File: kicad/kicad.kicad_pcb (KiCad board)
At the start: 2 copper layers, 50.8 x 25.4 mm, 13 parts, among them J1 USB_A_MALE, U1 MCP1702, U2 MCP6021

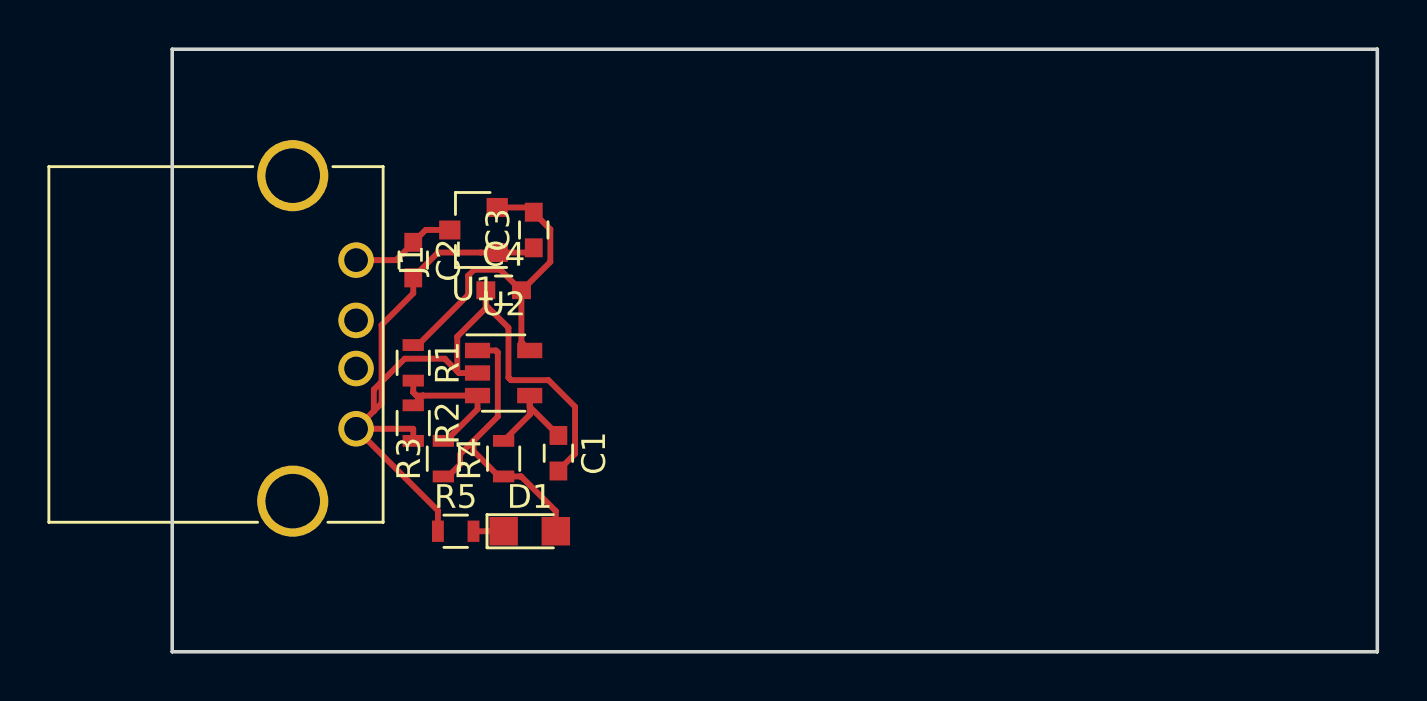
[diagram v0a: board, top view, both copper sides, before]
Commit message: Added fill of ground plane on front
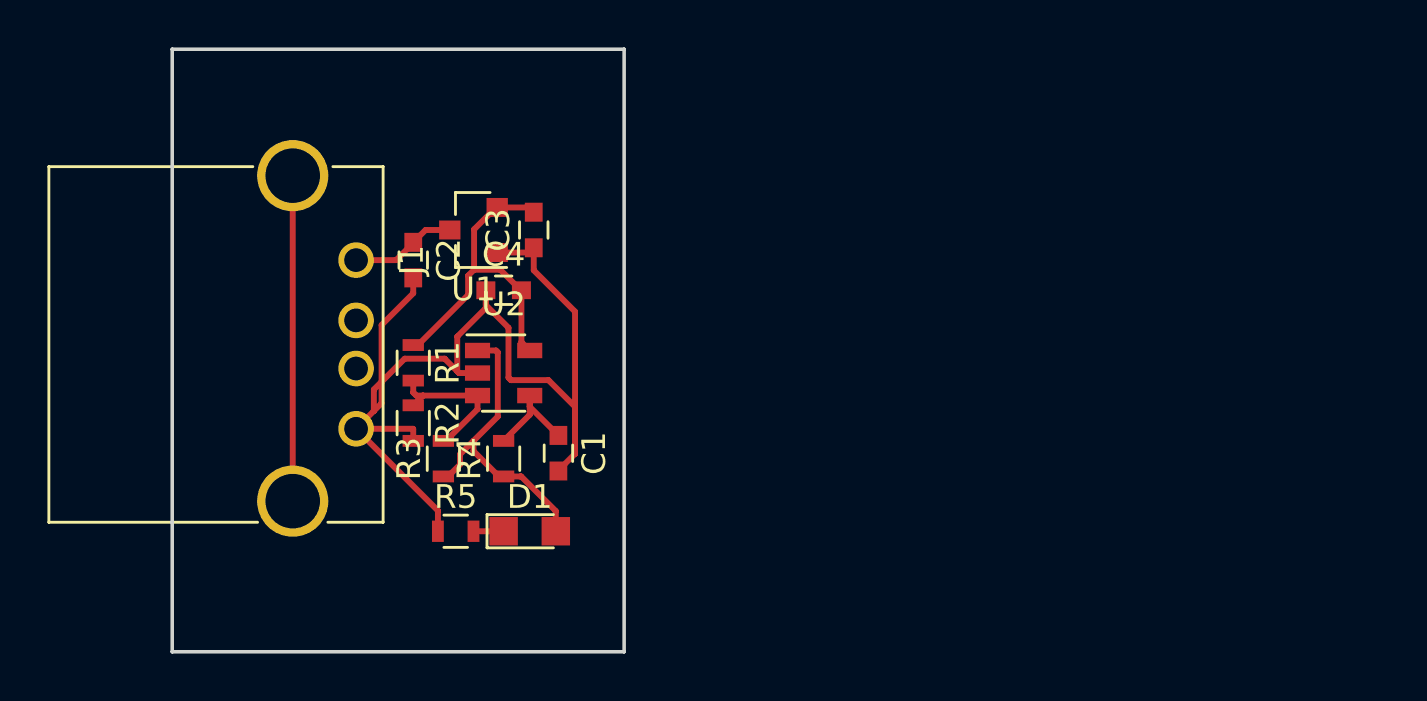
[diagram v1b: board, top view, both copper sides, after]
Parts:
- C2: value 1 uf -> 10 uf
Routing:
- net Net-(J1-Pad5): track 0.00 -> 13.7 mm
- net GND: track 42.1 -> 47.6 mm
- net +3V3: track 15.1 -> 14.1 mm
- added copper zone on F.Cu, net GND
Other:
- board size 50.8 x 25.4 mm -> 19.1 x 25.4 mm
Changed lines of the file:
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@@
   (general
     (links 24)
-    (no_connects 1)
-    (area 138.43 74.93 190.5 101.6)
+    (no_connects 0)
+    (area 139.624999 76.124999 190.575001 101.675001)
     (thickness 1.6)
     (drawings 4)
-    (tracks 83)
+    (tracks 84)
     (zones 0)
     (modules 13)
@@
     (47 F.CrtYd user)
     (48 B.Fab user)
-    (49 F.Fab user)
+    (49 F.Fab user hide)
   )
   (setup
@@
       (effects (font (size 1 1) (thickness 0.15)))
     )
-    (fp_text value "1 uf" (at 0 1.5 270) (layer F.Fab)
+    (fp_text value "10 uf" (at 0 1.5 270) (layer F.Fab)
       (effects (font (size 1 1) (thickness 0.15)))
     )
@@
   )
   (gr_line (start 139.7 76.2) (end 139.7 101.6) (layer Edge.Cuts) (width 0.15))
-  (gr_line (start 190.5 76.2) (end 139.7 76.2) (layer Edge.Cuts) (width 0.15))
-  (gr_line (start 190.5 101.6) (end 190.5 76.2) (layer Edge.Cuts) (width 0.15))
-  (gr_line (start 139.7 101.6) (end 190.5 101.6) (layer Edge.Cuts) (width 0.15))
+  (gr_line (start 158.75 76.2) (end 139.7 76.2) (layer Edge.Cuts) (width 0.15))
+  (gr_line (start 158.75 101.6) (end 158.75 76.2) (layer Edge.Cuts) (width 0.15))
+  (gr_line (start 139.7 101.6) (end 158.75 101.6) (layer Edge.Cuts) (width 0.15))
+  (segment (start 154.94 84.57) (end 154.94 85.519998) (width 0.25) (layer F.Cu) (net 1))
+  (segment (start 154.94 85.519998) (end 156.680001 87.259999) (width 0.25) (layer F.Cu) (net 1))
+  (segment (start 156.680001 87.259999) (end 156.680001 93.254999) (width 0.25) (layer F.Cu) (net 1))
+  (segment (start 156.680001 93.254999) (end 155.98 93.955) (width 0.25) (layer F.Cu) (net 1))
+  (segment (start 155.98 93.955) (end 155.98 93.98) (width 0.25) (layer F.Cu) (net 1))
   (segment (start 149.86 85.84) (end 149.86 86.49) (width 0.25) (layer F.Cu) (net 1))
   (segment (start 149.86 86.49) (end 148.525001 87.824999) (width 0.25) (layer F.Cu) (net 1))
@@
   (segment (start 148.525001 91.124999) (end 148.199999 91.450001) (width 0.25) (layer F.Cu) (net 1))
   (segment (start 148.199999 91.450001) (end 147.45 92.2) (width 0.25) (layer F.Cu) (net 1))
-  (segment (start 155.98 93.98) (end 155.98 93.955) (width 0.25) (layer F.Cu) (net 1))
-  (segment (start 155.98 93.955) (end 156.680001 93.254999) (width 0.25) (layer F.Cu) (net 1))
   (segment (start 156.680001 93.254999) (end 156.680001 91.269999) (width 0.25) (layer F.Cu) (net 1))
   (segment (start 156.680001 91.269999) (end 155.560001 90.149999) (width 0.25) (layer F.Cu) (net 1))
@@
   (segment (start 154.74 84.77) (end 154.94 84.57) (width 0.25) (layer F.Cu) (net 1))
   (segment (start 149.86 85.84) (end 149.86 85.815) (width 0.25) (layer F.Cu) (net 1))
-  (segment (start 149.86 85.815) (end 150.905 84.77) (width 0.25) (layer F.Cu) (net 1))
-  (segment (start 150.905 84.77) (end 152.7 84.77) (width 0.25) (layer F.Cu) (net 1))
-  (segment (start 152.7 84.77) (end 153.4 84.77) (width 0.25) (layer F.Cu) (net 1))
   (segment (start 154.77 90.8) (end 154.77 91.27) (width 0.25) (layer F.Cu) (net 2))
   (segment (start 154.77 91.27) (end 155.98 92.48) (width 0.25) (layer F.Cu) (net 2))
@@
   (segment (start 151.4 83.82) (end 150.38 83.82) (width 0.25) (layer F.Cu) (net 3))
   (segment (start 150.38 83.82) (end 149.86 84.34) (width 0.25) (layer F.Cu) (net 3))
+  (segment (start 153.4 82.87) (end 153.35 82.87) (width 0.25) (layer F.Cu) (net 4))
+  (segment (start 153.35 82.87) (end 152.424997 83.795003) (width 0.25) (layer F.Cu) (net 4))
+  (segment (start 152.424997 83.795003) (end 152.424997 85.495001) (width 0.25) (layer F.Cu) (net 4))
   (segment (start 154.94 83.07) (end 154.94 83.095) (width 0.25) (layer F.Cu) (net 4))
-  (segment (start 154.94 83.095) (end 155.640001 83.795001) (width 0.25) (layer F.Cu) (net 4))
-  (segment (start 155.640001 83.795001) (end 155.640001 85.164999) (width 0.25) (layer F.Cu) (net 4))
-  (segment (start 155.640001 85.164999) (end 154.445 86.36) (width 0.25) (layer F.Cu) (net 4))
   (segment (start 154.445 86.36) (end 154.42 86.36) (width 0.25) (layer F.Cu) (net 4))
   (segment (start 154.42 86.36) (end 154.42 88.55) (width 0.25) (layer F.Cu) (net 4))
@@
   (segment (start 153.425001 88.975001) (end 153.425001 91.684999) (width 0.25) (layer F.Cu) (net 5))
   (segment (start 152.4 96.52) (end 153.67 96.52) (width 0.25) (layer F.Cu) (net 6))
+  (segment (start 144.78 81.53) (end 144.78 95.25) (width 0.25) (layer F.Cu) (net 7))
   (segment (start 149.86 90.17) (end 149.86 90.67) (width 0.25) (layer F.Cu) (net 8))
   (segment (start 149.86 90.67) (end 149.99 90.8) (width 0.25) (layer F.Cu) (net 8))
@@
   (segment (start 152.57 91.375) (end 151.235 92.71) (width 0.25) (layer F.Cu) (net 8))
   (segment (start 151.235 92.71) (end 151.13 92.71) (width 0.25) (layer F.Cu) (net 8))
+  (zone (net 1) (net_name GND) (layer F.Cu) (hatch edge 0.508)
+    (connect_pads (clearance 0.508))
+    (min_thickness 0.254)
+    (fill yes (arc_segments 16) (thermal_gap 0.508) (thermal_bridge_width 0.508))
+    (polygon
+      (pts
+        (xy 158.75 76.2) (xy 139.7 76.2) (xy 139.7 101.6) (xy 158.75 101.6)
+      )
+    )
+  )
 )

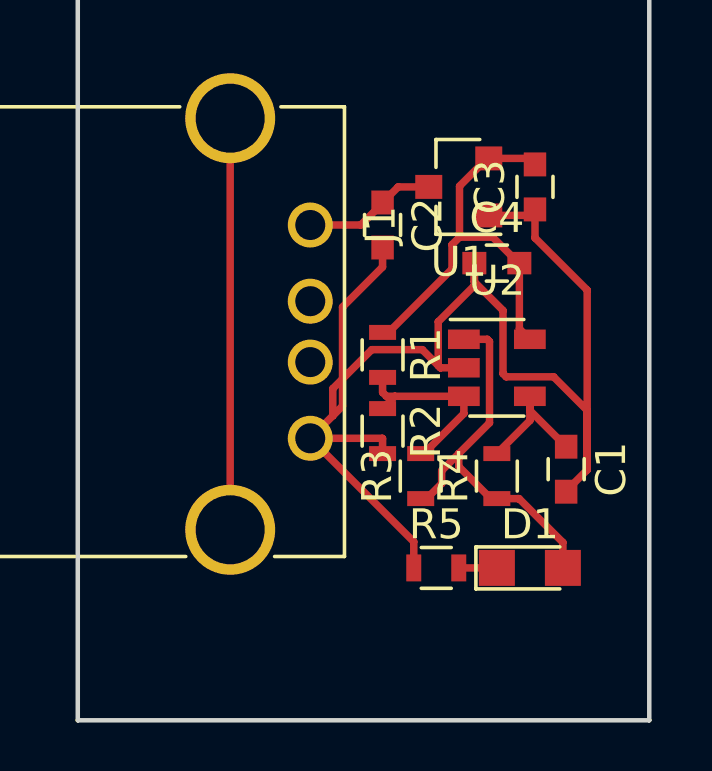
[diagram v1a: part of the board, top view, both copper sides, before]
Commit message: Fixed capacitor size for large caps
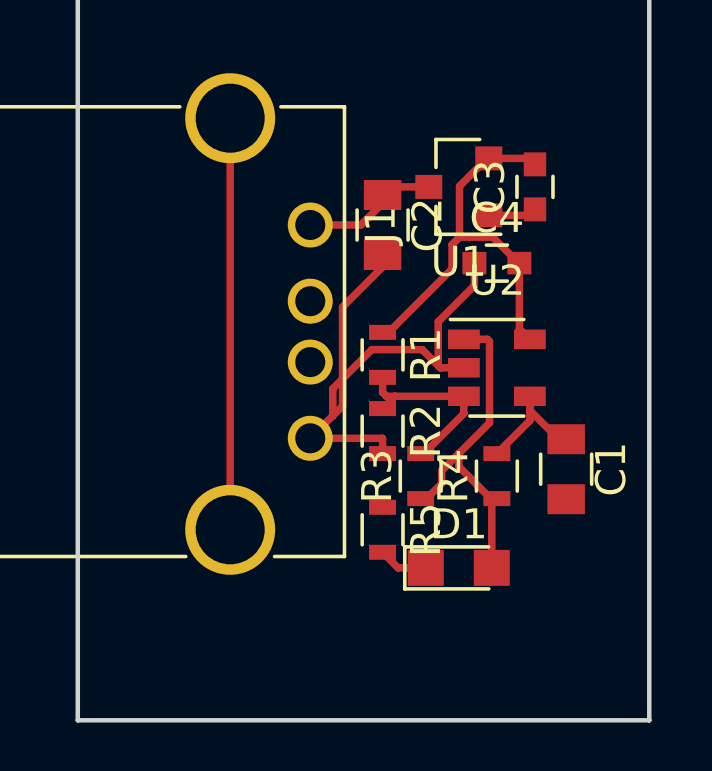
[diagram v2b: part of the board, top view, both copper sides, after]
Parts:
- C1: value C -> 10u; footprint Capacitors_SMD:C_0603 -> Capacitors_SMD:C_0805
- C2: footprint Capacitors_SMD:C_0603 -> Capacitors_SMD:C_0805
- R1: value 100k -> 95.3k
- R3: value 100k -> 110k
- R4: value R -> 80.6k
- moved D1 2.37 mm to (152.4, 96.5)
- moved R5 2.19 mm to (149.9, 95.2), turned to 270 degrees
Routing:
- net GND: track 47.6 -> 22.3 mm
- net /blink: track 13.0 -> 11.7 mm

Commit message: Layout stuff?
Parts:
- J1: footprint Connectors:USB_A -> usb_male:USB_A_male
- moved R5 10.9 mm to (151.9, 84.6)
- moved D1 9.91 mm to (149.3, 87.1), turned to 180 degrees
- moved J1 8.64 mm to (139.7, 88.9)
- moved C1 8.63 mm to (147.6, 95.2), turned to 180 degrees
- moved C4 5.59 mm to (148.8, 89.2)
- moved C3 5.29 mm to (149.9, 82.3), turned to 180 degrees
- moved U2 5.17 mm to (148.7, 91.2)
- moved C2 3.88 mm to (146.6, 83.1), turned to 180 degrees
- moved R4 3.64 mm to (150.1, 94.2), turned to 270 degrees
- moved R3 3.31 mm to (147.8, 93.5), turned to 180 degrees
- moved U1 3.14 mm to (149.4, 84.6)
- moved R1 1.80 mm to (151.6, 89.1)
- moved R2 1.80 mm to (151.6, 91.7), turned to 90 degrees
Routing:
- net GND: track 22.3 -> 43.5 mm
- net Net-(J1-Pad5): track 13.7 -> 0.00 mm
- net Net-(R1-Pad2): track 6.41 -> 15.2 mm
- net Net-(C2-Pad1): track 4.49 -> 11.3 mm
- net +3V3: track 14.1 -> 11.4 mm
- net /blink: track 11.7 -> 9.83 mm
- net Net-(D1-Pad1): track 1.66 -> 2.93 mm
- net Net-(C1-Pad1): track 4.55 -> 5.53 mm
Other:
- board size 19.1 x 25.4 mm -> 14 x 16.5 mm
- net class Power added: clearance 0.2, trace_width 0.4, via_dia 0.6, via_drill 0.4

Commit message: Finished layout
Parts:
- C1: value 10u -> 10 uf
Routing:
- net +3V3: track 11.4 -> 14.5 mm
- net GND: track 43.5 -> 41.3 mm
- net Net-(C2-Pad1): track 11.3 -> 11.8 mm
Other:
- rule trace_min: 0.2 -> 0.1524
- board text added: "Eric Miller"

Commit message: Exported sensitivity and schematic
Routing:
- net Net-(C2-Pad1): track 11.8 -> 11.3 mm
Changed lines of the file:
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@@
     (area 139.624999 80.569999 153.745001 97.230001)
     (thickness 1.6)
-    (drawings 5)
+    (drawings 7)
     (tracks 87)
     (zones 0)
@@
     )
   )
+  (dimension 15.24 (width 0.3) (layer F.SilkS)
+    (gr_text "15.240 mm" (at 128.952 88.9 90) (layer F.SilkS)
+      (effects (font (size 1.5 1.5) (thickness 0.3)))
+    )
+    (feature1 (pts (xy 134.366 81.28) (xy 127.602 81.28)))
+    (feature2 (pts (xy 134.366 96.52) (xy 127.602 96.52)))
+    (crossbar (pts (xy 130.302 96.52) (xy 130.302 81.28)))
+    (arrow1a (pts (xy 130.302 81.28) (xy 130.888421 82.406504)))
+    (arrow1b (pts (xy 130.302 81.28) (xy 129.715579 82.406504)))
+    (arrow2a (pts (xy 130.302 96.52) (xy 130.888421 95.393496)))
+    (arrow2b (pts (xy 130.302 96.52) (xy 129.715579 95.393496)))
+  )
+  (dimension 6.604 (width 0.3) (layer F.SilkS)
+    (gr_text "6.604 mm" (at 143.002 102.442) (layer F.SilkS)
+      (effects (font (size 1.5 1.5) (thickness 0.3)))
+    )
+    (feature1 (pts (xy 139.7 99.822) (xy 139.7 103.792)))
+    (feature2 (pts (xy 146.304 99.822) (xy 146.304 103.792)))
+    (crossbar (pts (xy 146.304 101.092) (xy 139.7 101.092)))
+    (arrow1a (pts (xy 139.7 101.092) (xy 140.826504 100.505579)))
+    (arrow1b (pts (xy 139.7 101.092) (xy 140.826504 101.678421)))
+    (arrow2a (pts (xy 146.304 101.092) (xy 145.177496 100.505579)))
+    (arrow2b (pts (xy 146.304 101.092) (xy 145.177496 101.678421)))
+  )
   (gr_text "Eric Miller" (at 140.716 88.9 270) (layer F.SilkS)
     (effects (font (size 1.4 1.2) (thickness 0.25)))
@@
   (segment (start 150.927999 93.084999) (end 149.979 92.136) (width 0.25) (layer F.Cu) (net 2) (status 20))
   (segment (start 149.979 92.136) (end 149.774 92.136) (width 0.25) (layer F.Cu) (net 2) (status 30))
+  (segment (start 148.352 84.582) (end 148.352 83.852) (width 0.4) (layer F.Cu) (net 3) (status 10))
+  (segment (start 148.352 83.852) (end 147.558 83.058) (width 0.4) (layer F.Cu) (net 3) (status 20))
   (segment (start 148.352 84.582) (end 148.352 85.04) (width 0.4) (layer F.Cu) (net 3) (status 10))
   (segment (start 148.352 85.04) (end 145.750001 87.641999) (width 0.4) (layer F.Cu) (net 3))
@@
   (segment (start 145.750001 91.199999) (end 144.55 92.4) (width 0.4) (layer F.Cu) (net 3) (status 20))
   (segment (start 148.352 84.582) (end 148.302 84.582) (width 0.4) (layer F.Cu) (net 3) (status 30))
-  (segment (start 148.352 84.582) (end 148.352 83.344) (width 0.4) (layer F.Cu) (net 3) (status 10))
-  (segment (start 148.352 83.344) (end 147.558 82.55) (width 0.4) (layer F.Cu) (net 3) (status 20))
   (segment (start 149.367999 84.566001) (end 149.367999 87.376) (width 0.4) (layer F.Cu) (net 4))
   (segment (start 149.367999 87.376) (end 149.367999 88.164999) (width 0.4) (layer F.Cu) (net 4))
-  (segment (start 149.774 90.236) (end 149.774 88.448002) (width 0.4) (layer F.Cu) (net 4))
+  (segment (start 149.774 90.236) (end 149.774 88.448002) (width 0.4) (layer F.Cu) (net 4) (status 10))
   (segment (start 149.774 88.448002) (end 149.367999 88.042001) (width 0.4) (layer F.Cu) (net 4))
   (segment (start 149.367999 88.042001) (end 149.367999 87.376) (width 0.4) (layer F.Cu) (net 4))
